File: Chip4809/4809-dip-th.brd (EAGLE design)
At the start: 57.9 x 20 mm, 20 parts, among them Q1 32768

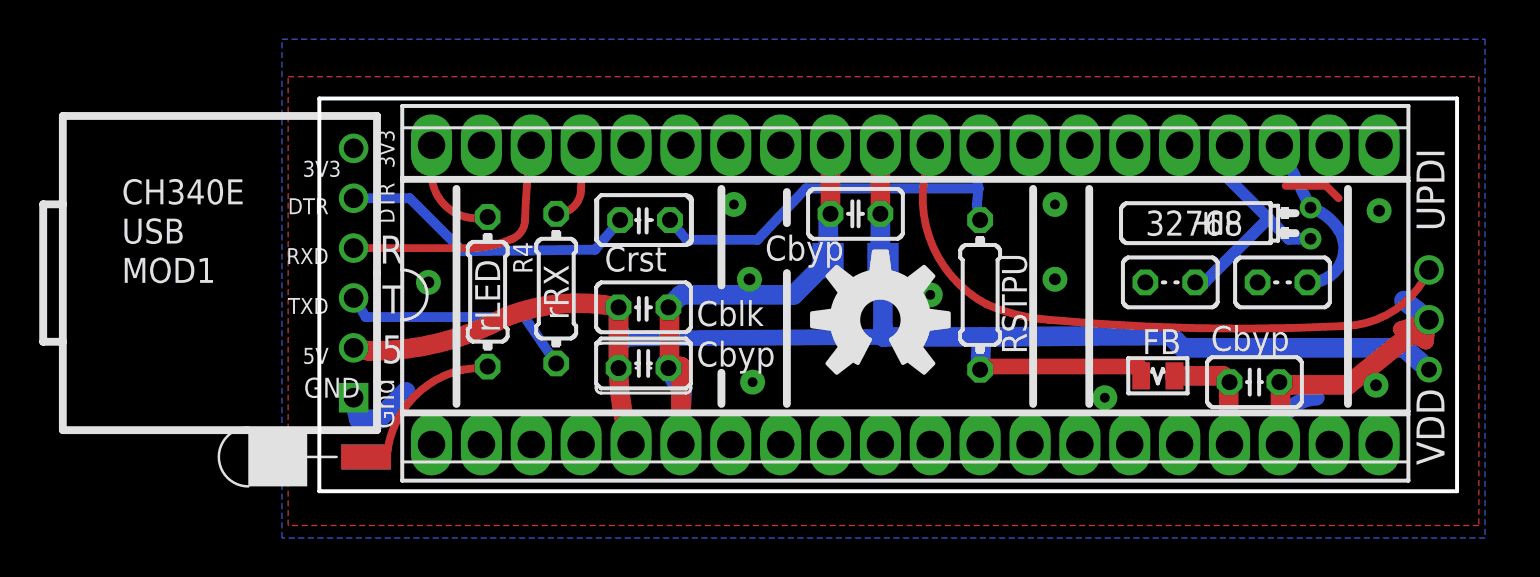
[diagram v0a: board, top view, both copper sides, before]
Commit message: Version 0.4 fix RX/TX, move UPDI pin
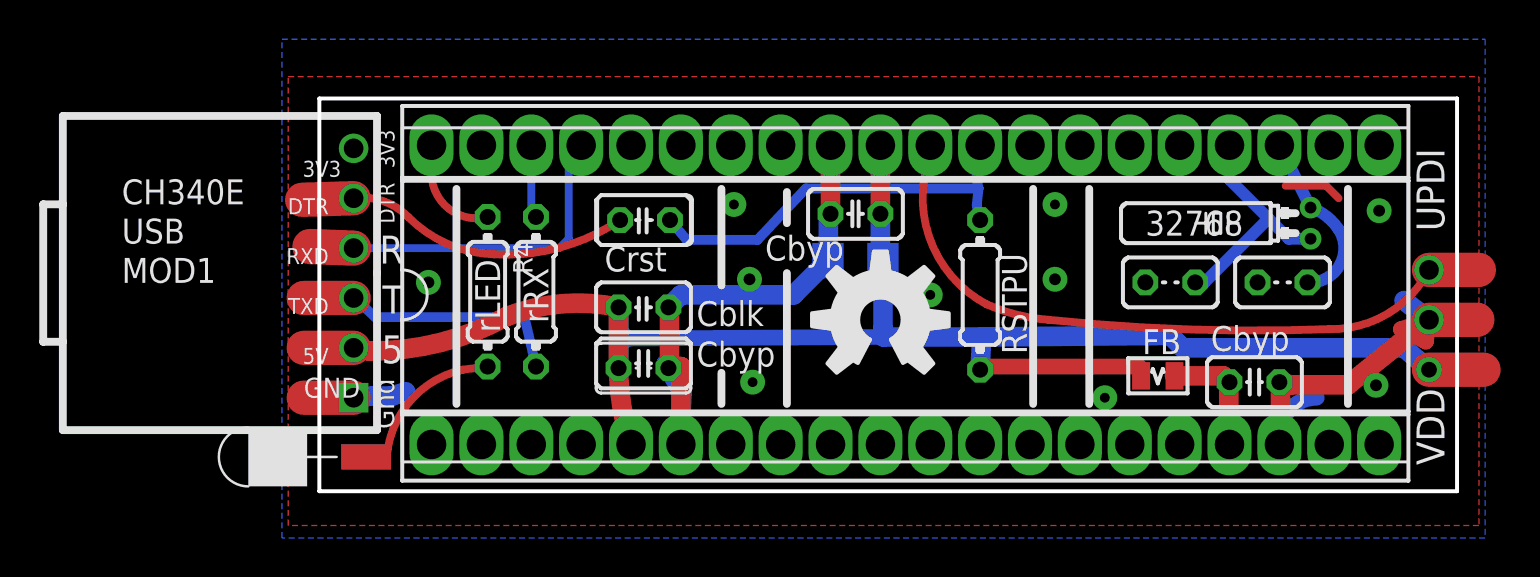
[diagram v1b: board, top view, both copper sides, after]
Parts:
- R4: value RxIso -> rLED
- VS1: value 0.2 -> 0.3
- moved R1 1.04 mm to (39.6, 45.9)
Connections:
- removed net CPURX: R1.2, U$1.37
- removed net CPUTX: MOD1.RX, U$1.38
- new net N$3: R1.2, U$1.38
- new net N$4: MOD1.RX, U$1.37
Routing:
- net N$4: track 0.00 -> 18.4 mm
- net CPUTX: track 13.1 -> 0.00 mm
- net VCC: track 86.1 -> 91.4 mm
- net CPURX: track 4.02 -> 0.00 mm
- net N$3: track 0.00 -> 3.75 mm
- net GND: track 55.3 -> 58.9 mm
- net UPDI: track 32.1 -> 34.6 mm
- net USBTX: track 12.1 -> 14.2 mm
- net N$8: track 15.4 -> 17.0 mm
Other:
- board text added: "20190830 by WestfW: RX/TX reversed, damn it. Fix."
